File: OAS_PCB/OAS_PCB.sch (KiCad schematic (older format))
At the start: 47 parts

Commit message: updated the DAC wiring
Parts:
- added C? (x3): 10 µ, symbol Device:CP1_Small
- added C? (x3): 1 µ, symbol Device:CP1_Small
- added C? (x3): .1µ, symbol Device:C
- added D? (x6): 1N4002, Diode_THT:D_DO-41_SOD81_P10.16mm_Horizontal, symbol Diode:1N4002
- added R? (x3): 360, symbol Device:R
- added R? (x3): 120, symbol Device:R
- added U? (x3): LM317_TO-220, Package_TO_SOT_THT:TO-220-3_Vertical, symbol Regulator_Linear:LM317_TO-220
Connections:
- net labels added: -5V(NeedsCalculating), 0, 3V(NeedsCalculating)
- wire segments 167 -> 257
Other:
- moved on the sheet: DAC?

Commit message: did some work on PCB schematic
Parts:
- removed C? (x3): 10 µ, symbol Device:CP1_Small
- removed C? (x3): 1 µ, symbol Device:CP1_Small
- removed C? (x3): .1µ, symbol Device:C
- removed D? (x6): 1N4002, Diode_THT:D_DO-41_SOD81_P10.16mm_Horizontal, symbol Diode:1N4002
- removed R? (x3): 360, symbol Device:R
- removed R? (x3): 120, symbol Device:R
- removed U? (x3): LM317_TO-220, Package_TO_SOT_THT:TO-220-3_Vertical, symbol Regulator_Linear:LM317_TO-220
- added -5VSupply: LM337_TO220, Package_TO_SOT_THT:TO-220-3_Vertical, symbol Regulator_Linear:LM337_TO220
- added C?: 1 µ, symbol Device:CP1_Small
- added C?: 10 µ, symbol Device:CP1_Small
- added C?: .1µ, symbol Device:C
- added D? (x2): 1N4002, Diode_THT:D_DO-41_SOD81_P10.16mm_Horizontal, symbol Diode:1N4002
- added R?: 120, symbol Device:R
- added R?: 360, symbol Device:R
- U?: symbol teensy:Teensy4.0 -> OAS_PCB-rescue:Teensy4.0-teensy
- gave numbers to parts that had none: 1
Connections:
- net labels added: -5V(needsCalculating)
- net labels removed: -5V(NeedsCalculating), 0, 3V(NeedsCalculating)
- wire segments 257 -> 212
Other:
- note added: "Vref-Reference input voltage; 3 V to AVDD.\nVout-DAC output voltage; output swing is ±VREF\nOSRS1&2-Digital input for selecting the oversampling ratio (2,4,8,16)\nBPB-Active-low, asynchronous digital input for filter bypass\nFSYNC-Digital input. FSYNC is word clock\nRSTB-Filter reset. Active-low, asynchronous digital input for disabling all digital filter activity."
- moved on the sheet: +5VSupply, C?, D?, J?, R?, U?

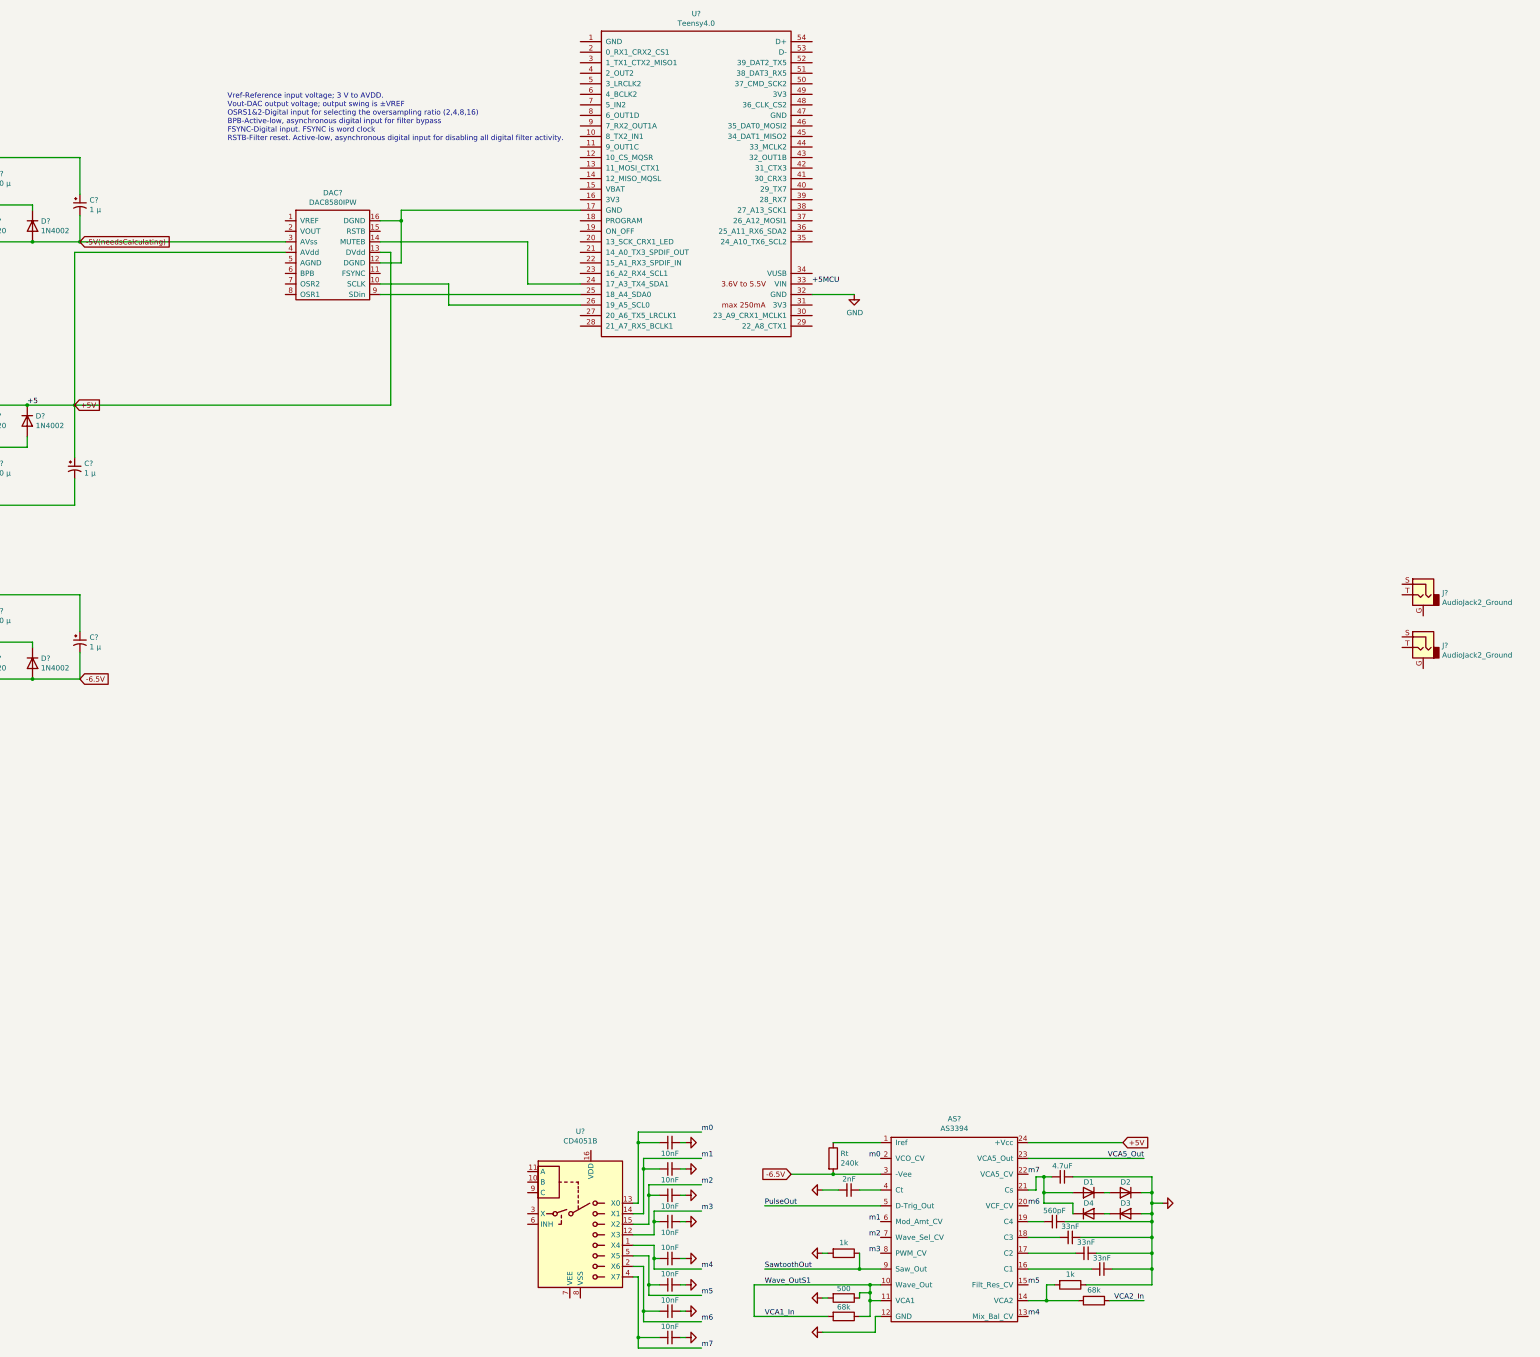
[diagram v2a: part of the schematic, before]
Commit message: checked -5 v supply, connected Vout and Vref on DAC
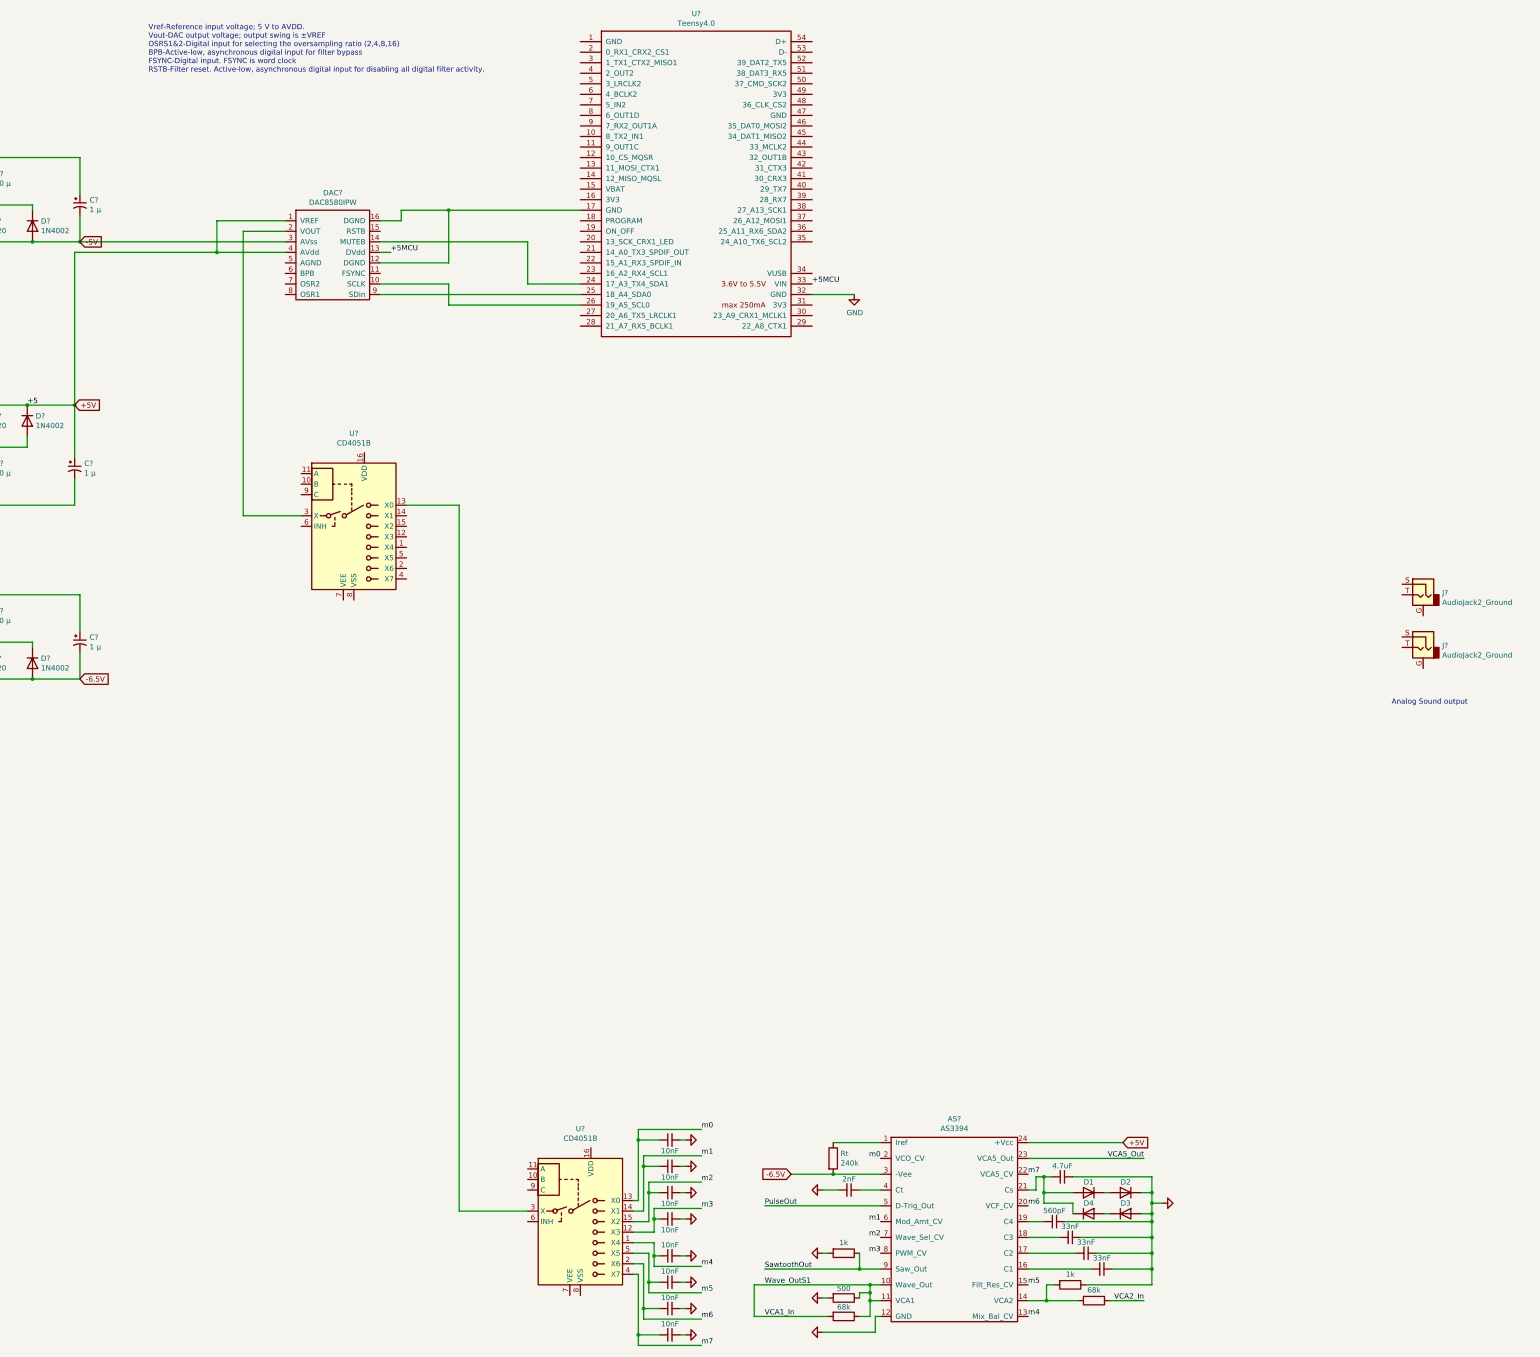
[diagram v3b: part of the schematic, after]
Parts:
- added U?: CD4051B, symbol Analog_Switch:CD4051B
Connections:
- net +5MCU: now also DAC?.13 (DVdd)
- net +5V: now also DAC?.1 (VREF); no longer DAC?.13 (DVdd)
- net at U?.3 (X): now also U?.13 (X0)
- net at DAC?.2 (VOUT): now also U?.3 (X)
- net -5V(needsCalculating) renamed -5V
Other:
- note added: "Analog Sound output"
- note added: "Vref-Reference input voltage; 5 V to AVDD.\nVout-DAC output voltage; output swing is ±VREF\nOSRS1&2-Digital input for selecting the oversampling ratio (2,4,8,16)\nBPB-Active-low, asynchronous digital input for filter bypass\nFSYNC-Digital input. FSYNC is word clock\nRSTB-Filter reset. Active-low, asynchronous digital input for disabling all digital filter activity."
- note removed: "Vref-Reference input voltage; 3 V to AVDD.\nVout-DAC output voltage; output swing is ±VREF\nOSRS1&2-Digital input for selecting the oversampling ratio (2,4,8,16)\nBPB-Active-low, asynchronous digital input for filter bypass\nFSYNC-Digital input. FSYNC is word clock\nRSTB-Filter reset. Active-low, asynchronous digital input for disabling all digital filter activity."
- moved on the sheet: U?

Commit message: Add global net labels.
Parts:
- removed J?: AudioJack2_Ground, symbol Connector:AudioJack2_Ground
- added R?: 68k, symbol Device:R
- added U1: TL072, symbol Amplifier_Operational:TL072
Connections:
- net +12 renamed +12V
- net +5MCU renamed +5Digital
- net -12 renamed -12V
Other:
- moved on the sheet: J?
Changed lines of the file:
@@
 	1    0    0    -1
 $EndComp
-Text Label 5400 5650 0    50   ~ 0
-+12
-Text Label 5400 8250 0    50   ~ 0
--12
 Text Notes 4200 7450 2    50   ~ 0
 Power_input
@@
 Wire Wire Line
 	6250 7500 6250 7450
-Text Label 4750 7250 0    50   ~ 0
-+12
-Text Label 4750 7550 0    50   ~ 0
--12
 $Comp
 L power:GND #PWR?
@@
 Wire Wire Line
 	4750 7450 5100 7450
-Text Label 4750 7350 0    50   ~ 0
-+5MCU
 $Comp
 L Device:C C?
@@
 L Connector:AudioJack2_Ground J?
 U 1 1 602102C1
-P 20400 7450
-F 0 "J?" H 20220 7468 50  0000 R CNN
-F 1 "AudioJack2_Ground" H 20220 7377 50  0000 R CNN
-F 2 "" H 20400 7450 50  0001 C CNN
-F 3 "~" H 20400 7450 50  0001 C CNN
-	1    20400 7450
-	-1   0    0    -1
-$EndComp
-$Comp
-L Connector:AudioJack2_Ground J?
-U 1 1 602145F4
-P 20400 7950
-F 0 "J?" H 20220 7968 50  0000 R CNN
-F 1 "AudioJack2_Ground" H 20220 7877 50  0000 R CNN
-F 2 "" H 20400 7950 50  0001 C CNN
-F 3 "~" H 20400 7950 50  0001 C CNN
-	1    20400 7950
+P 20250 9100
+F 0 "J?" H 20070 9118 50  0000 R CNN
+F 1 "AudioJack2_Ground" H 20070 9027 50  0000 R CNN
+F 2 "" H 20250 9100 50  0001 C CNN
+F 3 "~" H 20250 9100 50  0001 C CNN
+	1    20250 9100
 	-1   0    0    -1
 $EndComp
@@
 	1    0    0    -1
 $EndComp
-Text Label 14600 4500 0    50   ~ 0
-+5MCU
 $Comp
 L power:GND #PWR?
@@
 	1    0    0    -1
 $EndComp
-Text Label 5400 4100 0    50   ~ 0
--12
 Connection ~ 5750 4100
 Wire Wire Line
@@
 -5V
 Wire Wire Line
-	9600 4100 7650 4100
-Connection ~ 7650 4100
-Wire Wire Line
 	9600 4200 8950 4200
-Wire Wire Line
-	7600 4200 7600 5650
-Connection ~ 7600 5650
 Wire Wire Line
 	10500 4200 10600 4200
@@
 	1    0    0    -1
 $EndComp
-Text Label 10600 4200 0    50   ~ 0
-+5MCU
 Wire Wire Line
 	11150 4300 11150 3800
@@
 Wire Wire Line
 	8950 3900 9600 3900
-Connection ~ 8950 4200
-Wire Wire Line
-	8950 4200 7600 4200
 Wire Wire Line
 	10750 6600 11250 6600
 Wire Wire Line
 	11250 13300 11900 13300
-Text Notes 20100 8500 0    50   ~ 0
+Text Notes 20000 9600 0    50   ~ 0
 Analog Sound output
 Wire Wire Line
 	11250 6600 11250 13300
+$Comp
+L Amplifier_Operational:TL072 U1
+U 1 1 6022EA93
+P 19000 9500
+F 0 "U1" H 19000 9867 50  0000 C CNN
+F 1 "TL072" H 19000 9776 50  0000 C CNN
+F 2 "" H 19000 9500 50  0001 C CNN
+F 3 "http://www.ti.com/lit/ds/symlink/tl071.pdf" H 19000 9500 50  0001 C CNN
+	1    19000 9500
+	1    0    0    -1
+$EndComp
+$Comp
+L Amplifier_Operational:TL072 U1
+U 3 1 6023EABE
+P 19700 7500
+F 0 "U1" H 19658 7546 50  0000 L CNN
+F 1 "TL072" H 19658 7455 50  0000 L CNN
+F 2 "" H 19700 7500 50  0001 C CNN
+F 3 "http://www.ti.com/lit/ds/symlink/tl071.pdf" H 19700 7500 50  0001 C CNN
+	3    19700 7500
+	1    0    0    -1
+$EndComp
+$Comp
+L Amplifier_Operational:TL072 U1
+U 2 1 6025C5CA
+P 19000 10150
+F 0 "U1" H 19000 10517 50  0000 C CNN
+F 1 "TL072" H 19000 10426 50  0000 C CNN
+F 2 "" H 19000 10150 50  0001 C CNN
+F 3 "http://www.ti.com/lit/ds/symlink/tl071.pdf" H 19000 10150 50  0001 C CNN
+	2    19000 10150
+	1    0    0    -1
+$EndComp
+Text GLabel 4750 7250 2    50   Input ~ 0
++12V
+Text GLabel 4750 7550 2    50   Input ~ 0
+-12V
+Text GLabel 5150 7350 2    50   Input ~ 0
++5Digital
+Wire Wire Line
+	4750 7350 5150 7350
+Text GLabel 10600 4200 2    50   Input ~ 0
++5Digital
+Text GLabel 14900 4500 2    50   Input ~ 0
++5Digital
+Wire Wire Line
+	14600 4500 14900 4500
+Text GLabel 5400 8250 0    50   Input ~ 0
+-12V
+Text GLabel 5400 5650 0    50   Input ~ 0
++12V
+Text GLabel 5400 4100 0    50   Input ~ 0
+-12V
+Text GLabel 9600 4100 0    50   Input ~ 0
+-5V
+Text GLabel 8950 3900 0    50   Input ~ 0
++5V
+$Comp
+L Device:R R?
+U 1 1 602E50A2
+P 18450 10550
+F 0 "R?" V 18243 10550 50  0001 C CNN
+F 1 "68k" V 18350 10550 50  0000 C CNN
+F 2 "" V 18380 10550 50  0001 C CNN
+F 3 "~" H 18450 10550 50  0001 C CNN
+	1    18450 10550
+	-1   0    0    1
+$EndComp
 $EndSCHEMATC

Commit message: did some work on the PCB, going to get with Jacob today regarding the Teensy and then complete the wiring for that
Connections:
- net Teensy: now reaches DAC?.11 (FSYNC)
- net Teensy: now also DAC?.15 (RSTB), DAC?.6 (BPB), DAC?.7 (OSR2), DAC?.8 (OSR1)
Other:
- note added: "ANALOG SYNTH VOICE CHIP\n"
- note added: "DAC & TEENSY \n"
- note added: "DAC OUTPUT MULTIPLEXERS\n"
- note added: "Power Supply & Voltage Regulators"
- moved on the sheet: +5VSupply, -5VSupply, AS?, C?, D1, D2, D3, D4, D?, DAC?, J?, R?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
